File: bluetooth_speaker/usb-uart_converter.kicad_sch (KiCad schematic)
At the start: 6 parts, among them U3 CP2102N-A01-GQFN28

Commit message: adding few footprints
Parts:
- C21, C22: footprint (none) -> Capacitor_SMD:C_0603_1608Metric_Pad1.08x0.95mm_HandSolder
- R4, R6: footprint (none) -> Resistor_SMD:R_0603_1608Metric_Pad0.98x0.95mm_HandSolder
- R5: footprint (none) -> Resistor_SMD:R_0603_1608Metric_Pad0.98x0.95mm_HandSolderResistor_SMD:R_0603_1608Metric_Pad0.98x0.95mm_HandSolder
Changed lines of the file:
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@@
 			)
 		)
-		(property "Footprint" ""
+		(property "Footprint" "Resistor_SMD:R_0603_1608Metric_Pad0.98x0.95mm_HandSolderResistor_SMD:R_0603_1608Metric_Pad0.98x0.95mm_HandSolder"
 			(at 27.432 78.74 90)
 			(effects
@@
 			)
 		)
-		(property "Footprint" ""
+		(property "Footprint" "Resistor_SMD:R_0603_1608Metric_Pad0.98x0.95mm_HandSolder"
 			(at 27.432 67.31 90)
 			(effects
@@
 			)
 		)
-		(property "Footprint" ""
+		(property "Footprint" "Resistor_SMD:R_0603_1608Metric_Pad0.98x0.95mm_HandSolder"
 			(at 50.292 85.09 90)
 			(effects
@@
 			)
 		)
-		(property "Footprint" ""
+		(property "Footprint" "Capacitor_SMD:C_0603_1608Metric_Pad1.08x0.95mm_HandSolder"
 			(at 34.29 43.18 0)
 			(effects
@@
 			)
 		)
-		(property "Footprint" ""
+		(property "Footprint" "Capacitor_SMD:C_0603_1608Metric_Pad1.08x0.95mm_HandSolder"
 			(at 22.86 43.18 0)
 			(effects

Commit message: Completed adding footprints, set up PCB rules
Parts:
- R5: footprint Resistor_SMD:R_0603_1608Metric_Pad0.98x0.95mm_HandSolderResistor_SMD:R_0603_1608Metric_Pad0.98x0.95mm_HandSolder -> Resistor_SMD:R_0603_1608Metric_Pad0.98x0.95mm_HandSolder
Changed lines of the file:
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@@
 			)
 		)
-		(property "Footprint" "Resistor_SMD:R_0603_1608Metric_Pad0.98x0.95mm_HandSolderResistor_SMD:R_0603_1608Metric_Pad0.98x0.95mm_HandSolder"
+		(property "Footprint" "Resistor_SMD:R_0603_1608Metric_Pad0.98x0.95mm_HandSolder"
 			(at 27.432 78.74 90)
 			(effects

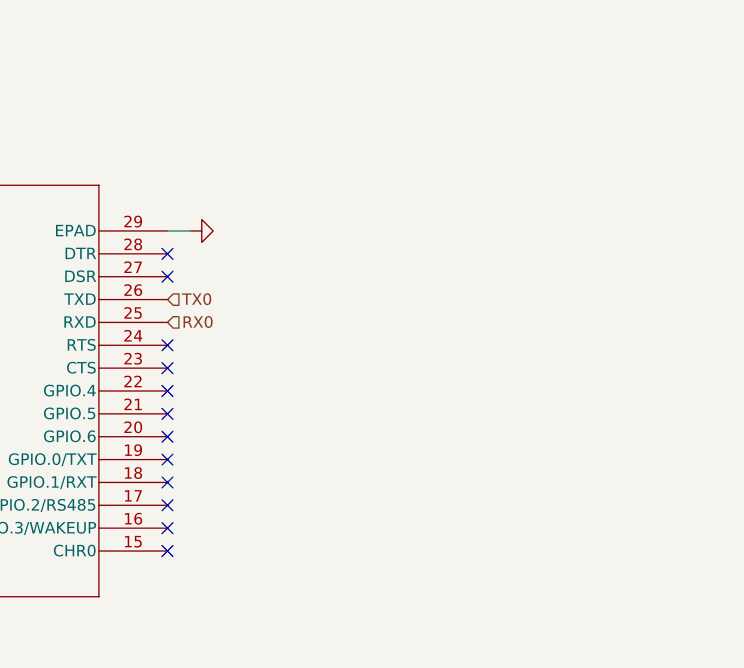
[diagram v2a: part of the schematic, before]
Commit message: Added auto-programming through CP2102
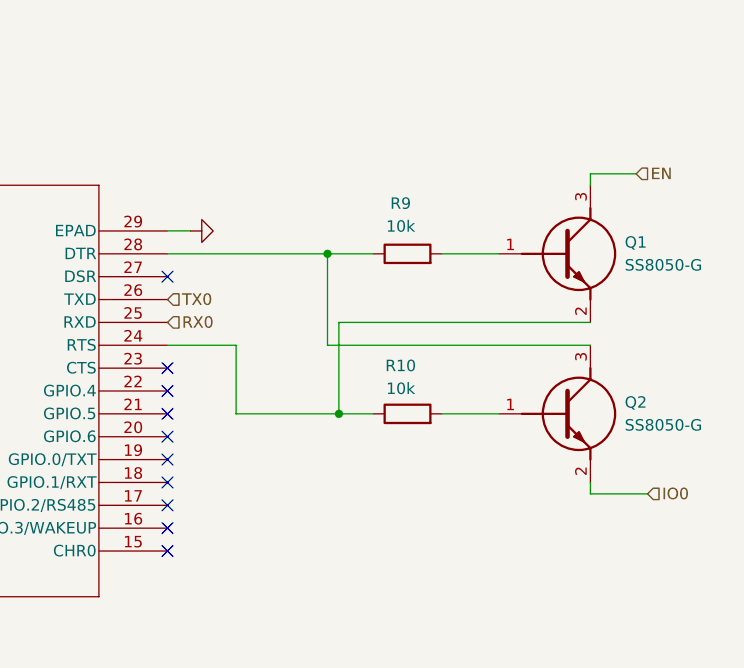
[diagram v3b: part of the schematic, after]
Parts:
- added Q1, Q2: SS8050-G, SOT95P240X115-3N, symbol SamacSys_Parts:SS8050-G
- added R10, R9: 10k, Resistor_SMD:R_0603_1608Metric_Pad0.98x0.95mm_HandSolder, symbol Device:R
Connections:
- net at U3.24 (RTS): now also Q1.2 (E), R10.1
- net at U3.28 (DTR): now also Q2.3 (C), R9.1
- new net: Q1.1 (B), R9.2
- new net: Q2.1 (B), R10.2
- new net EN: Q1.3 (C)
- new net IO0: Q2.2 (E)
- no-connect marks 19 -> 17

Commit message: Completed the PCB design
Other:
- company: (none) -> Politechnika Poznańska
- title: (none) -> bluetooth speaker
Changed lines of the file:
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@@
 	(generator_version "9.0")
 	(paper "A4")
+	(title_block
+		(title "bluetooth speaker")
+		(date "2026-01-05")
+		(rev "1.0")
+		(company "Politechnika Poznańska")
+	)
 	(text "USB-UART converter"
 		(exclude_from_sim no)

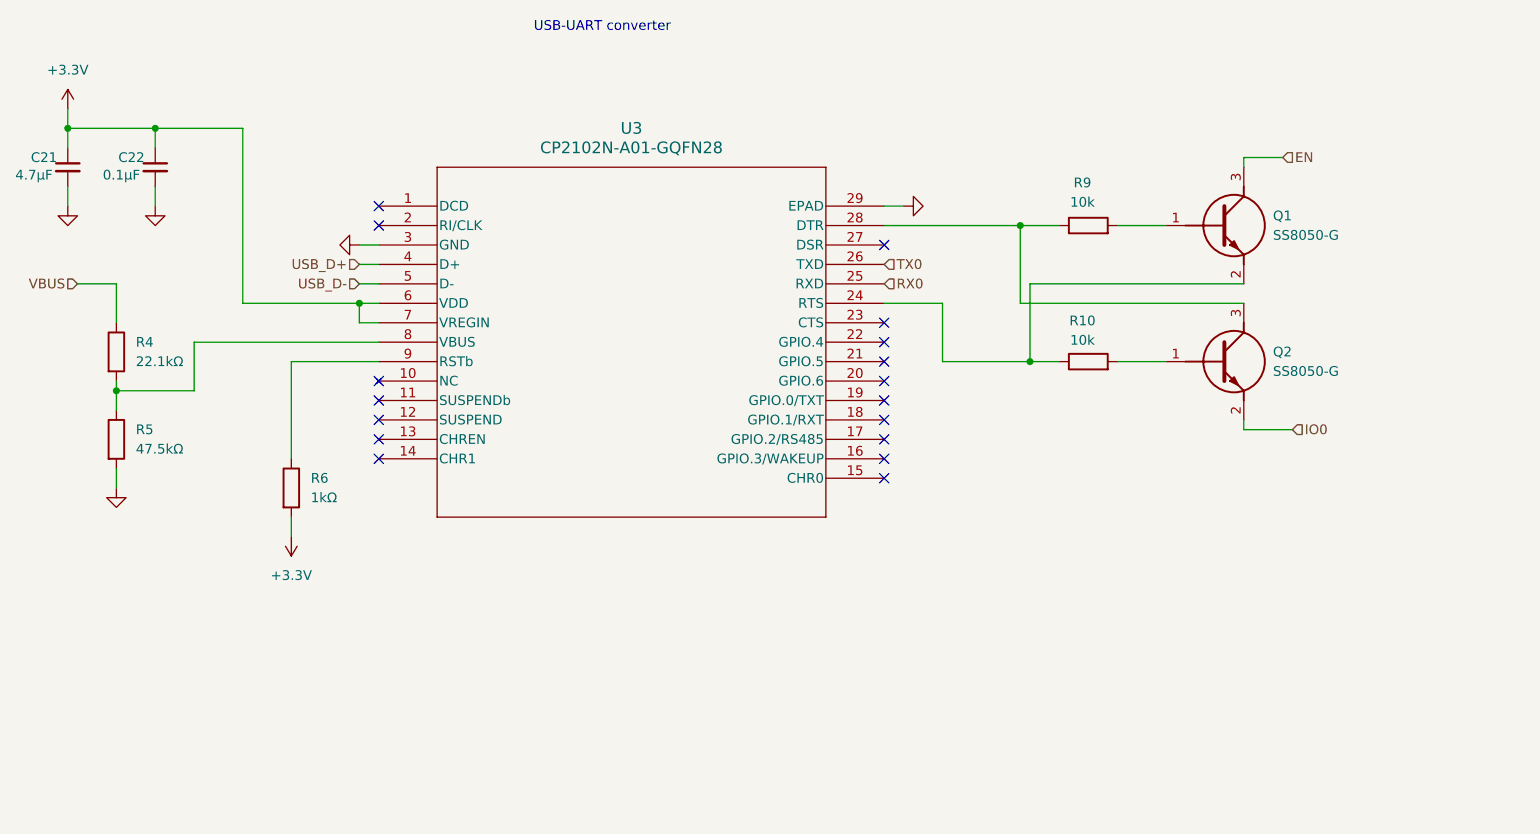
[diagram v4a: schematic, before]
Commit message: Exchanged CP2102N to CP2102C due to discontinuation
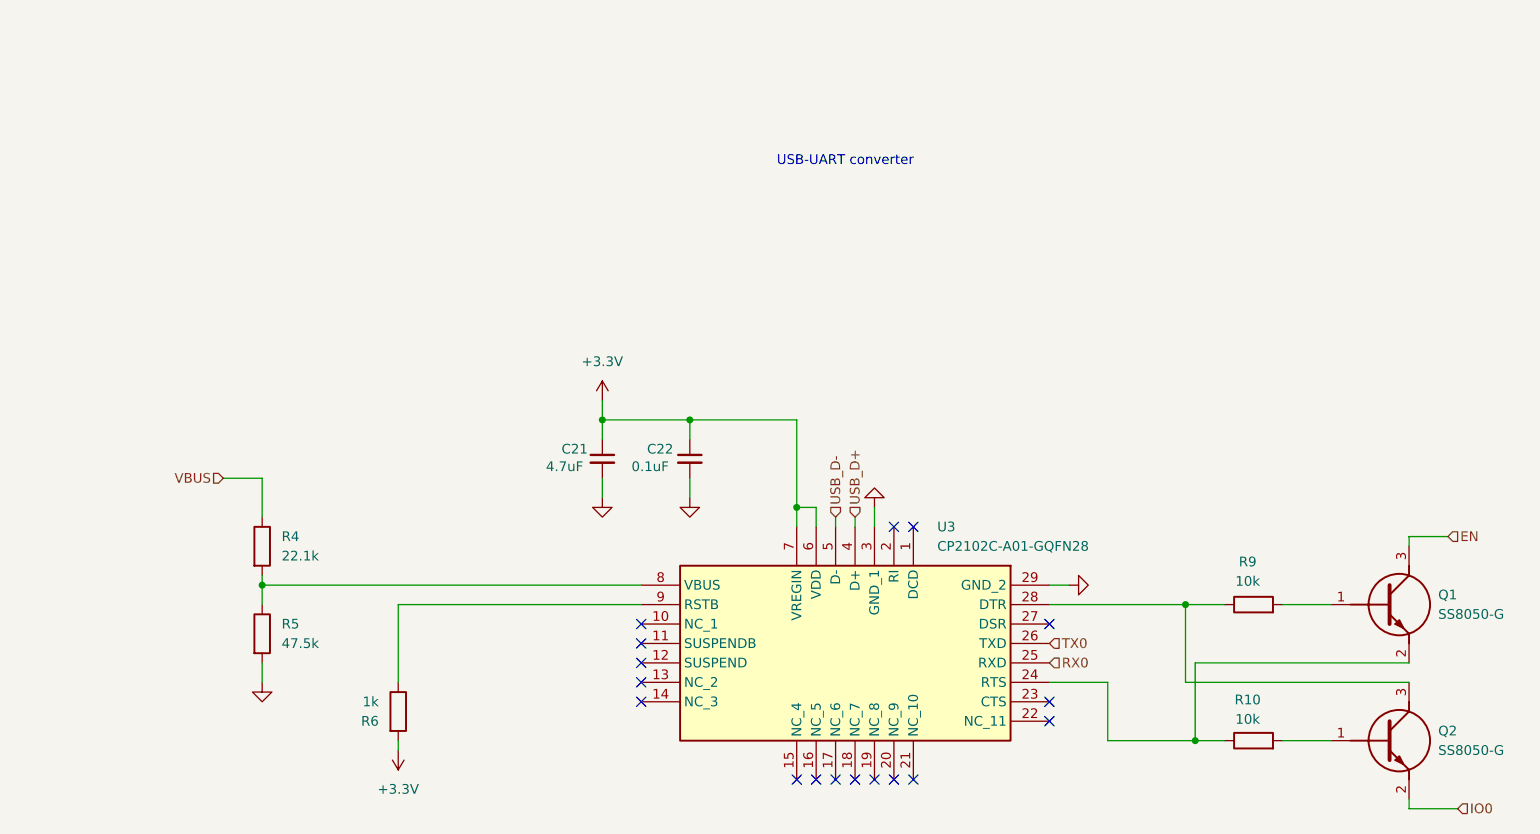
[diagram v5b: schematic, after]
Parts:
- removed U3: CP2102N-A01-GQFN28, CP2102N-A01-GQFN28:QFN28_5X5_SIL, symbol CP2102N-A01-GQFN28:CP2102N-A01-GQFN28
- added U3: CP2102C-A01-GQFN28, QFN50P500X500X80-29N-D, symbol SamacSys_Parts:CP2102C-A01-GQFN28
- C21: value 4.7µF -> 4.7uF
- C22: value 0.1µF -> 0.1uF
- R4: value 22.1kΩ -> 22.1k
- R5: value 47.5kΩ -> 47.5k
- R6: value 1kΩ -> 1k
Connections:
- net +3.3V: now also U3.6 (VDD), U3.7 (VREGIN)
- net GND: now also U3.29 (GND_2), U3.3 (GND_1)
- net RX0: now also U3.25 (RXD)
- net TX0: now also U3.26 (TXD)
- net USB_D+: now also U3.4 (D+)
- net USB_D-: now also U3.5 (D-)
- net at R4.2, R5.1: now also U3.8 (VBUS)
- net at Q2.3 (C), R9.1: now also U3.28 (DTR)
- net at Q1.2 (E), R10.1: now also U3.24 (RTS)
- net at R6.1: now also U3.9 (RSTB)
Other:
- moved on the sheet: C21, C22
